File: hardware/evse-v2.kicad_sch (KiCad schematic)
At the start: 178 parts, among them P1 TP VCCPWR, P10 TP DC-X6, P103 N+L, P11 TP DC-X30, P12 TP PE, P13 TP L', P14 TP A, P15 TP B, P16 TP 5V, P17 TP GND, P18 TP CS, P19 TP CLK, P2 TP 5V, P20 TP MOSI, P21 TP MISO, P22 TP GND, P23 TP N, P24 TP REL, P25 TP OUTA, P26 TP OUTB, P27 TP M SW, P28 TP GND, P29 TP EN, P3 TP GND, P30 TP GND, P31 TP VCCPWR, P32 TP GND, P33 TP SW, P34 TP SWLED, P35 TP GPIO IN, P36 TP GPIO OUT, P37 TP CP, P38 TP PE, P39 TP PP, P4 TP L, P5 TP DC-5V, P6 TP N, P7 TP GND, P8 TP DC-ERR, P9 TP DC-TST

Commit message: Version 2.7: Changed L103 to 0 Ohm resistor.
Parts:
- removed L105: (no value), symbol tinkerforge:INDUCTOR
- added R1: 0, kicad-libraries:R1210, symbol tinkerforge:R
- A101, A102, A103, A104: value (none) -> DRILL; footprint (none) -> kicad-libraries:DRILL_NP_35
- A105, A106: value (none) -> Rail; footprint (none) -> kicad-libraries:din-rail-mount
- C101: value (none) -> 220pF; footprint (none) -> kicad-libraries:C0402F
- C102, C127, C130: value (none) -> 100nF; footprint (none) -> C0603F
- C103, C106, C107, C124, C125, C126: value (none) -> 1uF; footprint (none) -> kicad-libraries:C0603F
- C104, C105, C108, C109: value (none) -> 4.7uF/50V; footprint (none) -> kicad-libraries:C1206
- C110: value (none) -> 2.2uF; footprint (none) -> kicad-libraries:C0603F
- C111: value (none) -> 100uF; footprint (none) -> kicad-libraries:C1210
- C112, C113, C116, C117, C118, C119: value (none) -> 100nF/30V; footprint (none) -> kicad-libraries:C0603F
- C114: value (none) -> 10uF; footprint (none) -> kicad-libraries:C1206
- C120, C121: value (none) -> DNP; footprint (none) -> kicad-libraries:C0402F
- C128, C129: value (none) -> 10pF; footprint (none) -> C0603F
- C131: value (none) -> 220nF; footprint (none) -> C0603F
- C132: value (none) -> 100nF; footprint (none) -> kicad-libraries:C0603F
- D101, D102, D104, D107, D110, D113, D114: value (none) -> ‎PESD3V3L1BA; footprint (none) -> kicad-libraries:SOD-323
- D103: value (none) -> blue; footprint (none) -> kicad-libraries:D0603F
- D105, D108, D109: value (none) -> SMF4L13CA; footprint (none) -> kicad-libraries:SOD-123FL
- D106, D111: value (none) -> SMAJ24CA; footprint (none) -> DO-214AC
- D112: value (none) -> B0520LW-7; footprint (none) -> kicad-libraries:SOD-123
- D115, D116: value (none) -> 1N4007; footprint (none) -> kicad-libraries:DO-41
- F101, F102: value (none) -> FUSE; footprint (none) -> kicad-libraries:Fuse-Holder-5x20
- J101: value (none) -> Boot; footprint (none) -> kicad-libraries:SolderJumper
- L101, L103: value (none) -> FB; footprint (none) -> kicad-libraries:R0603F
- L102: value (none) -> NR3015T6R8M; footprint (none) -> kicad-libraries:NR3030
- L104: value (none) -> WE-SL; footprint (none) -> kicad-libraries:WE-SL
- P101: value (none) -> CON-SENSOR2; footprint (none) -> kicad-libraries:CON-SENSOR2_180
- P102: value (none) -> Relay; footprint (none) -> kicad-libraries:LSF-SMT-500-02-135
- P103: footprint (none) -> kicad-libraries:wm_2491620000
- P104: value (none) -> L'+PE; footprint (none) -> kicad-libraries:wm_2491620000
- P105: value (none) -> CP/PP/PE; footprint (none) -> kicad-libraries:OQ_4P_Vertical
- P106: value (none) -> Power; footprint (none) -> kicad-libraries:JST-PH-3-THT
- P107: value (none) -> Motor; footprint (none) -> kicad-libraries:JST-PH-4-THT
- P108: value (none) -> Switch_LED; footprint (none) -> kicad-libraries:JST-PH-5-THT
- P109: value (none) -> Enable; footprint (none) -> kicad-libraries:JST-PH-3-THT
- P110: value (none) -> MODBUS; footprint (none) -> kicad-libraries:JST-PH-4-THT
- P111: value (none) -> Debug; footprint (none) -> kicad-libraries:DEBUG_PAD
- P112: value (none) -> DC-Protect; footprint (none) -> kicad-libraries:CON-SENSOR2_180
- P113: value (none) -> GP; footprint (none) -> kicad-libraries:JST-PH-4-THT
- PTC101: value (none) -> PTC 0.45A; footprint (none) -> C1206
- Q101, Q103, Q104: value (none) -> 2N7002P; footprint (none) -> kicad-libraries:SOT23GDS
- Q102: value (none) -> SI2305CDS-T1-GE3; footprint (none) -> kicad-libraries:SOT23GDS
- Q105: value (none) -> SSM3J355R,LF; footprint (none) -> kicad-libraries:SOT23GDS
- R101: value (none) -> 100; footprint (none) -> kicad-libraries:R0603F
- R102, R110, R125: value (none) -> 75k; footprint (none) -> kicad-libraries:R0603F
- R103, R112, R119, R121, R132, R139, R140: value (none) -> 10k; footprint (none) -> kicad-libraries:R0603F
- R104, R108, R126, R129: value (none) -> 300k; footprint (none) -> kicad-libraries:R0603F
- R105, R106, R109, R122, R127, R130: value (none) -> 100k; footprint (none) -> kicad-libraries:R0603F
- R107: value (none) -> 910; footprint (none) -> kicad-libraries:R0603F
- R111, R115, R117, R120, R123, R124, R131, R138: value (none) -> 1k; footprint (none) -> kicad-libraries:R0603F
- R113, R128: value (none) -> MOV-10D391KTR; footprint (none) -> kicad-libraries:VAR_10mm
- R114: value (none) -> 120; footprint (none) -> kicad-libraries:R0805E
- R116, R118: value (none) -> RNF12FTD249K; footprint (none) -> kicad-libraries:RNF12-2
- R133: value (none) -> 47k; footprint (none) -> kicad-libraries:R0603F
- R134, R136: value (none) -> 750; footprint (none) -> R0603F
- R135: value (none) -> DNP; footprint (none) -> R0603F
- R137: value (none) -> 120; footprint (none) -> R0805E
- R141: value (none) -> 2k; footprint (none) -> kicad-libraries:R0603F
- REL101: value (none) -> AGQ200S12Z; footprint (none) -> kicad-libraries:AGQ2X0
- RP101: value (none) -> 82; footprint (none) -> kicad-libraries:4X0402
- RP102: value (none) -> 10k; footprint (none) -> kicad-libraries:0603X4
- RP103, RP104: value (none) -> 1k; footprint (none) -> kicad-libraries:4X0603
- RP105: value (none) -> 10k; footprint (none) -> kicad-libraries:4X0603
- SW101, SW102: value (none) -> OS103011MS8QP1; footprint (none) -> kicad-libraries:OS103011MS8QP1
- U101: value (none) -> XMC1404; footprint (none) -> kicad-libraries:QFN48-EP2
- U102: value (none) -> PEM1-S12-D12-S; footprint (none) -> kicad-libraries:PEM1S
- U103: value (none) -> DMMT5401; footprint (none) -> kicad-libraries:SOT26
- U105: value (none) -> OPA171AIDBV; footprint (none) -> kicad-libraries:SOT23-5
- U106: value (none) -> A5950GLP; footprint (none) -> kicad-libraries:TSSOP16_EP
- U108: value (none) -> AQH3213AX; footprint (none) -> kicad-libraries:AQ-H
- U109: value (none) -> HCPL2731; footprint (none) -> kicad-libraries:DIP-8
- U110: value (none) -> TPS70933DBVR; footprint (none) -> kicad-libraries:SOT23-5
- U111: value (none) -> IRM02-12; footprint (none) -> kicad-libraries:IRM02
- U112: value (none) -> WPMDL110; footprint (none) -> kicad-libraries:WPMDL110
- U113: value (none) -> SP3491; footprint (none) -> kicad-libraries:SOIC-14_3.9x8.7mm_Pitch1.27mm
- X101: value (none) -> 16MHz; footprint (none) -> kicad-libraries:CRYSTAL_3225
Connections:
- net 5V: now also R1.1
- net at P112.6, P5.1: now also R1.2

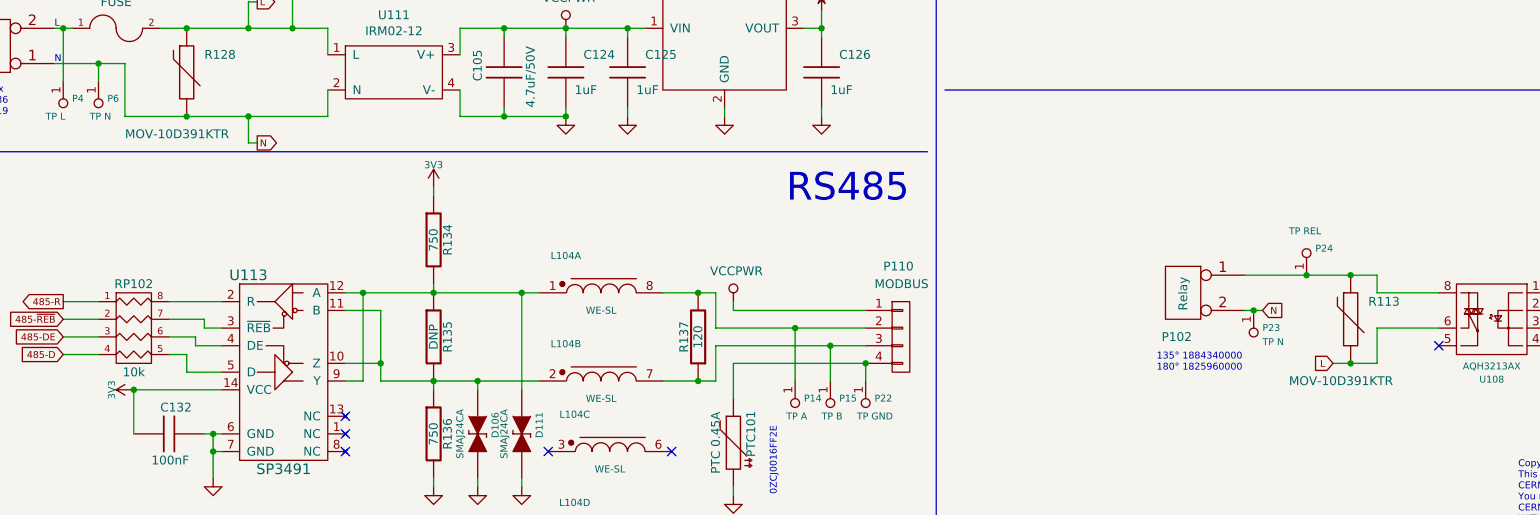
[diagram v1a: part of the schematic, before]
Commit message: change varistor
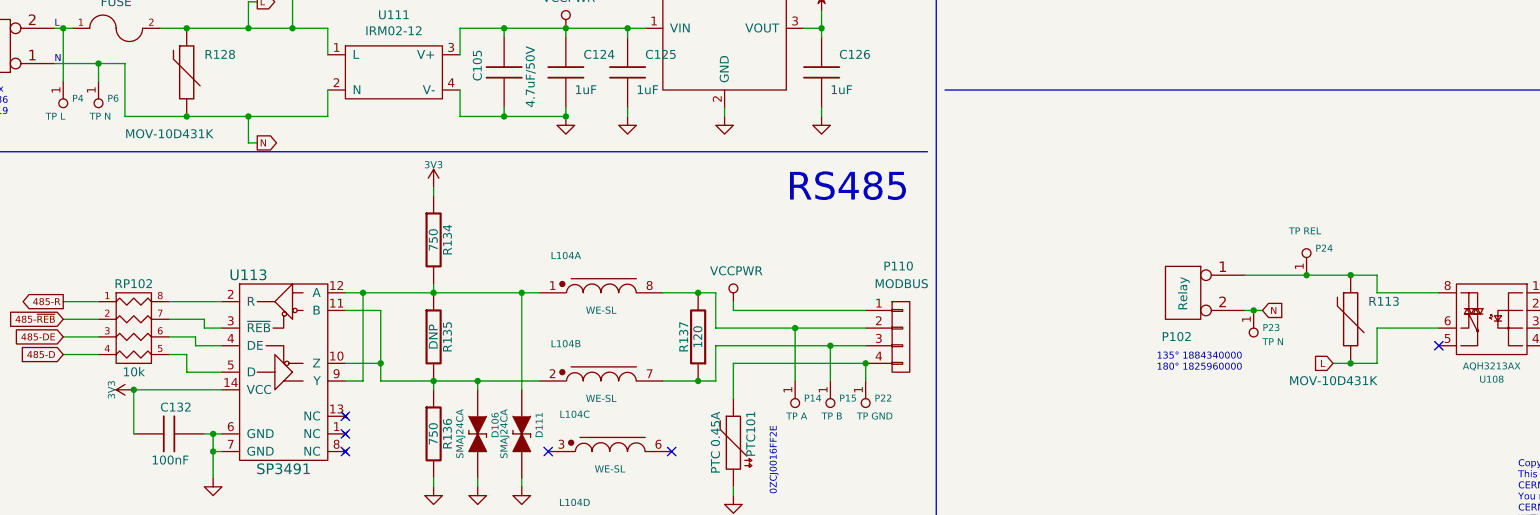
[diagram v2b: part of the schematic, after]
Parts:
- R113, R128: value MOV-10D391KTR -> MOV-10D431K
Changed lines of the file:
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@@
       (effects (font (size 1.27 1.27)) (justify left))
     )
-    (property "Value" "MOV-10D391KTR" (id 1) (at 205.74 257.81 0)
+    (property "Value" "MOV-10D431K" (id 1) (at 205.74 257.81 0)
       (effects (font (size 1.27 1.27)) (justify left))
     )
@@
       (effects (font (size 1.27 1.27)) (justify left))
     )
-    (property "Value" "MOV-10D391KTR" (id 1) (at 38.1 222.25 0)
+    (property "Value" "MOV-10D431K" (id 1) (at 38.1 222.25 0)
       (effects (font (size 1.27 1.27)) (justify left))
     )
@@
     )
     (path "/00000000-0000-0000-0000-00005f1d52c5"
-      (reference "R113") (unit 1) (value "MOV-10D391KTR") (footprint "kicad-libraries:VAR_10mm")
+      (reference "R113") (unit 1) (value "MOV-10D431K") (footprint "kicad-libraries:VAR_10mm")
     )
     (path "/00000000-0000-0000-0000-00005f24aeba"
@@
     )
     (path "/00000000-0000-0000-0000-0000608308b3"
-      (reference "R128") (unit 1) (value "MOV-10D391KTR") (footprint "kicad-libraries:VAR_10mm")
+      (reference "R128") (unit 1) (value "MOV-10D431K") (footprint "kicad-libraries:VAR_10mm")
     )
     (path "/00000000-0000-0000-0000-000060e12483"
